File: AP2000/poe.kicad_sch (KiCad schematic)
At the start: 70 parts, among them IC2 TPS23751PWPR, J11 Barrel_Jack, Q1 FDS86242, U12 HMHA2801AR2, U6 TL431AIDBVR

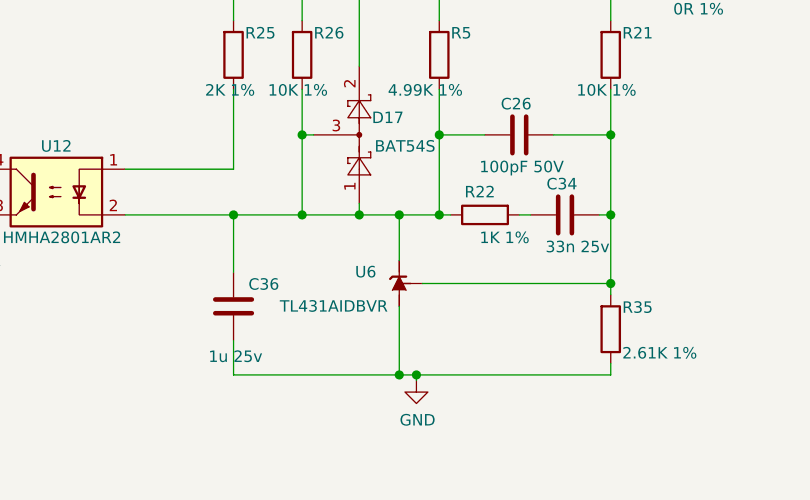
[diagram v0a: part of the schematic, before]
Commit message: Mods to AP2000 for manufacturing. 50 PCBs ordered from JLCPCB with SMd assembly.
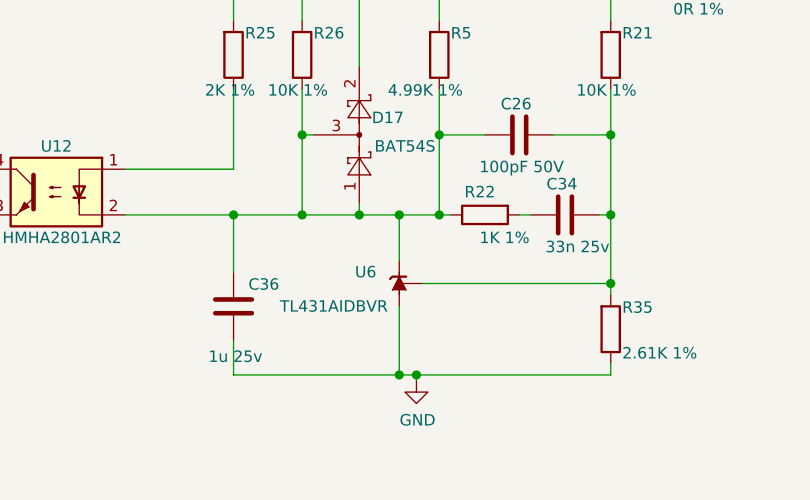
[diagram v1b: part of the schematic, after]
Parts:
- D10, D11, D12, D13, D4, D5, D6, D7, D8: LCSC C526416 -> C388246
- D17: LCSC C47546 -> C727126
- Q1: LCSC C57665 -> C148410
- U6: footprint Package_TO_SOT_SMD:SOT-23-5 -> Package_TO_SOT_SMD:SOT-23; symbol Reference_Voltage:TL431DBV -> Reference_Voltage:TL431DBZ; LCSC C144392 -> C23892
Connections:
- net GND: now also U6.3 (A); no longer U6.5 (A)
- net at C26.2, C34.2, R21.1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: now also U6.2 (REF); no longer U6.4 (REF)
- net at C26.1, C36.1, D17.1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: now also U6.1 (K); no longer U6.3 (K)
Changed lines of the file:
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@@
       (effects (font (size 1.27 1.27)) (justify left bottom) hide)
     )
-    (property "LCSC" "C526416" (id 12) (at 59.69 30.48 0)
+    (property "LCSC" "C388246" (id 12) (at 59.69 30.48 0)
       (effects (font (size 1.27 1.27)) hide)
     )
@@
       (effects (font (size 1.27 1.27)) (justify left bottom) hide)
     )
-    (property "LCSC" "C526416" (id 12) (at 59.69 48.26 0)
+    (property "LCSC" "C388246" (id 12) (at 59.69 48.26 0)
       (effects (font (size 1.27 1.27)) hide)
     )
@@
       (effects (font (size 1.27 1.27)) (justify left bottom) hide)
     )
-    (property "LCSC" "C526416" (id 12) (at 69.85 30.48 0)
+    (property "LCSC" "C388246" (id 12) (at 69.85 30.48 0)
       (effects (font (size 1.27 1.27)) hide)
     )
@@
       (effects (font (size 1.27 1.27)) (justify left bottom) hide)
     )
-    (property "LCSC" "C526416" (id 12) (at 69.85 48.26 0)
+    (property "LCSC" "C388246" (id 12) (at 69.85 48.26 0)
       (effects (font (size 1.27 1.27)) hide)
     )
@@
       (effects (font (size 1.27 1.27)) (justify left bottom) hide)
     )
-    (property "LCSC" "C526416" (id 12) (at 80.01 30.48 0)
+    (property "LCSC" "C388246" (id 12) (at 80.01 30.48 0)
       (effects (font (size 1.27 1.27)) hide)
     )
@@
       (effects (font (size 1.27 1.27)) (justify left bottom) hide)
     )
-    (property "LCSC" "C526416" (id 12) (at 80.01 48.26 0)
+    (property "LCSC" "C388246" (id 12) (at 80.01 48.26 0)
       (effects (font (size 1.27 1.27)) hide)
     )
@@
       (effects (font (size 1.27 1.27)) (justify left bottom) hide)
     )
-    (property "LCSC" "C526416" (id 12) (at 90.17 30.48 0)
+    (property "LCSC" "C388246" (id 12) (at 90.17 30.48 0)
       (effects (font (size 1.27 1.27)) hide)
     )
@@
       (effects (font (size 1.27 1.27)) (justify left bottom) hide)
     )
-    (property "LCSC" "C526416" (id 12) (at 90.17 48.26 0)
+    (property "LCSC" "C388246" (id 12) (at 90.17 48.26 0)
       (effects (font (size 1.27 1.27)) hide)
     )
@@
       (effects (font (size 1.27 1.27)) (justify left bottom) hide)
     )
-    (property "LCSC" "C526416" (id 12) (at 166.37 25.4 0)
+    (property "LCSC" "C388246" (id 12) (at 166.37 25.4 0)
       (effects (font (size 1.27 1.27)) hide)
     )
@@
     (pin "2")
   )
-  (symbol (lib_id "Reference_Voltage:TL431DBV") (at 224.155 146.05 270) (mirror x) (unit 1)
+  (symbol (lib_id "Reference_Voltage:TL431DBZ") (at 224.155 146.05 270) (mirror x) (unit 1)
     (in_bom yes) (on_board yes)
     (property "Reference" "U6" (id 0) (at 221.615 144.78 90)
@@
       (effects (font (size 1.27 1.27)) (justify right))
     )
-    (property "Footprint" "Package_TO_SOT_SMD:SOT-23-5" (id 2) (at 217.805 146.05 0)
+    (property "Footprint" "Package_TO_SOT_SMD:SOT-23" (id 2) (at 220.345 146.05 0)
       (effects (font (size 1.27 1.27) italic) hide)
     )
@@
       (effects (font (size 1.27 1.27)) hide)
     )
-    (property "LCSC" "C144392" (id 5) (at 224.155 146.05 0)
-      (effects (font (size 1.27 1.27)) hide)
-    )
+    (property "LCSC" "C23892" (id 5) (at 224.155 146.05 0)
+      (effects (font (size 1.27 1.27)) hide)
+    )
+    (pin "1")
+    (pin "2")
     (pin "3")
-    (pin "4")
-    (pin "5")
   )
   (symbol (lib_id "Device:C") (at 85.09 149.86 0) (unit 1)
@@
       (effects (font (size 1.27 1.27)) hide)
     )
-    (property "LCSC" "C47546" (id 5) (at 219.71 129.54 0)
+    (property "LCSC" "C727126" (id 5) (at 219.71 129.54 0)
       (effects (font (size 1.27 1.27)) hide)
     )
@@
       (effects (font (size 1.27 1.27)) (justify left) hide)
     )
-    (property "LCSC" "C57665" (id 12) (at 139.7 120.65 0)
-      (effects (font (size 1.27 1.27)) hide)
-    )
+    (property "LCSC" "C148410" (id 12) (at 139.7 120.65 0)
+      (effects (font (size 1.27 1.27)) hide)
+    )
